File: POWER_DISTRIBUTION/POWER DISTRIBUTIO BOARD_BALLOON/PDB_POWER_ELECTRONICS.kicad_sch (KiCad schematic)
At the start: 45 parts, among them IC7 TPS56837RPAR, U3 MP3432GL-P

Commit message: POWER BOARD LAYOUT COMPLETE
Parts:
- removed F1: 0154005.DRL, SamacSys_Parts:0154005DRL, symbol SamacSys_Parts:0154005.DRL
- added F2: 0154005.DRL, SamacSys_Parts:0154005DRL, symbol SamacSys_Parts:0154005.DRL
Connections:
- net VBAT+: now also F2.1
- net VBAT_Fused: now reaches C13.2, C15.2, C17.2, C19.2, PS3.1 (+VIN)
- net VBAT_Fused: now also F2.2

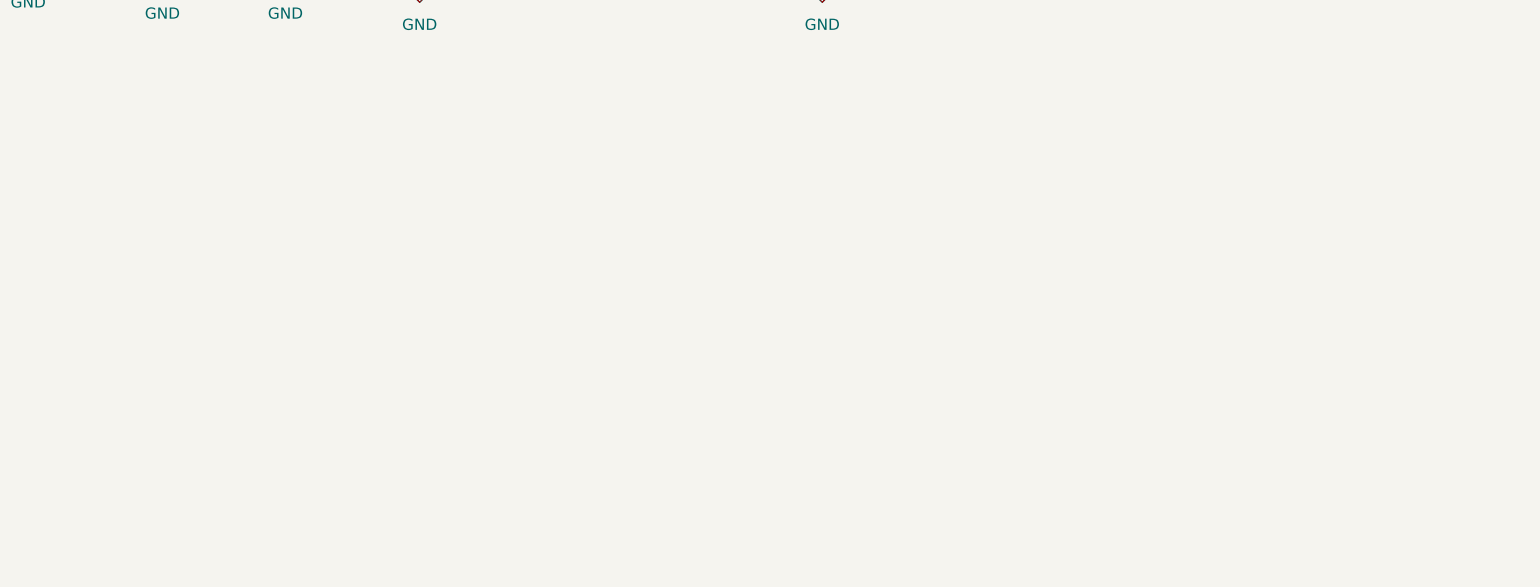
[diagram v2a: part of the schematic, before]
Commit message: almost finished wiring
btw for the i2c bus idk if it was meant to be SCL instead of SDL , there is alr an SDA line but i assume so
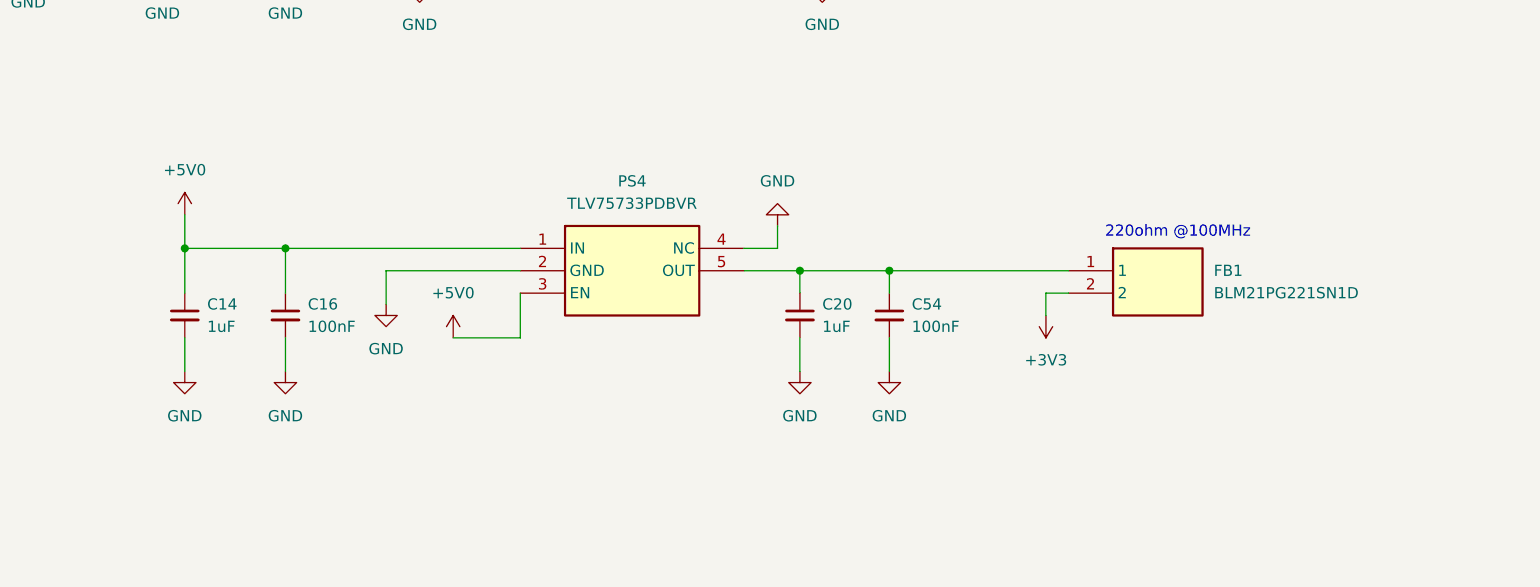
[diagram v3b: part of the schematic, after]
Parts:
- added C14, C20: 1uF, Capacitor_SMD:C_0603_1608Metric, symbol Device:C_Small
- added C16, C54: 100nF, Capacitor_SMD:C_0603_1608Metric, symbol Device:C_Small
- added FB1: BLM21PG221SN1D, SamacSys_COMMS:BEADC2012X105N, symbol Samac_sys:BLM21PG221SN1D
- added PS4: TLV75733PDBVR, SamacSys_COMMS:SOT95P280X145-5N, symbol Samac_sys:TLV75733PDBVR
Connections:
- net +5V0: now also C14.1, C16.1, PS4.1 (IN), PS4.3 (EN)
- net GND: now also C14.2, C16.2, C20.2, C54.2, PS4.2 (GND), PS4.4 (NC)
- new net: C20.1, C54.1, FB1.1, PS4.5 (OUT)
- new net +3V3: FB1.2
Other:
- note added: "220ohm @100MHz"

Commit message: revert commit
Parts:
- FB1: footprint SamacSys_COMMS:BEADC2012X105N -> SamacSys_Parts:BEADC2012X105N
- PS4: footprint SamacSys_COMMS:SOT95P280X145-5N -> SamacSys_Parts:SOT95P280X145-5N
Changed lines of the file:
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@@
 	)
 	(table
-		(column_count 1)
-		(border
-			(external yes)
-			(header yes)
-			(stroke
-				(width 0)
-				(type solid)
-			)
-		)
-		(separators
-			(rows yes)
-			(cols yes)
-			(stroke
-				(width 0)
-				(type solid)
-			)
-		)
-		(column_widths 19.05)
-		(row_heights -5.08)
-		(cells
-			(table_cell ""
-				(exclude_from_sim no)
-				(at 321.31 195.58 0)
-				(size 19.05 -5.08)
-				(margins 0.9525 0.9525 0.9525 0.9525)
-				(span 1 1)
-				(fill
-					(type none)
-				)
-				(effects
-					(font
-						(size 1.27 1.27)
-					)
-					(justify left top)
-				)
-			)
-		)
-	)
-	(table
 		(column_count 3)
 		(border
@@
 		)
 	)
+	(table
+		(column_count 1)
+		(border
+			(external yes)
+			(header yes)
+			(stroke
+				(width 0)
+				(type solid)
+			)
+		)
+		(separators
+			(rows yes)
+			(cols yes)
+			(stroke
+				(width 0)
+				(type solid)
+			)
+		)
+		(column_widths 19.05)
+		(row_heights -5.08)
+		(cells
+			(table_cell ""
+				(exclude_from_sim no)
+				(at 321.31 195.58 0)
+				(size 19.05 -5.08)
+				(margins 0.9525 0.9525 0.9525 0.9525)
+				(span 1 1)
+				(fill
+					(type none)
+				)
+				(effects
+					(font
+						(size 1.27 1.27)
+					)
+					(justify left top)
+				)
+			)
+		)
+	)
 	(global_label "MODE"
 		(shape output)
@@
 			)
 		)
-		(property "Footprint" "SamacSys_COMMS:BEADC2012X105N"
+		(property "Footprint" "SamacSys_Parts:BEADC2012X105N"
 			(at 186.69 178.74 0)
 			(effects
@@
 			)
 		)
-		(property "Footprint" "SamacSys_COMMS:SOT95P280X145-5N"
+		(property "Footprint" "SamacSys_Parts:SOT95P280X145-5N"
 			(at 129.54 176.2 0)
 			(effects

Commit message: test
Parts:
- FB1: footprint SamacSys_Parts:BEADC2012X105N -> SamacSys_COMMS:BEADC2012X105N
- PS4: footprint SamacSys_Parts:SOT95P280X145-5N -> SamacSys_COMMS:SOT95P280X145-5N
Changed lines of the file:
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@@
 	)
 	(table
+		(column_count 1)
+		(border
+			(external yes)
+			(header yes)
+			(stroke
+				(width 0)
+				(type solid)
+			)
+		)
+		(separators
+			(rows yes)
+			(cols yes)
+			(stroke
+				(width 0)
+				(type solid)
+			)
+		)
+		(column_widths 19.05)
+		(row_heights -5.08)
+		(cells
+			(table_cell ""
+				(exclude_from_sim no)
+				(at 321.31 195.58 0)
+				(size 19.05 -5.08)
+				(margins 0.9525 0.9525 0.9525 0.9525)
+				(span 1 1)
+				(fill
+					(type none)
+				)
+				(effects
+					(font
+						(size 1.27 1.27)
+					)
+					(justify left top)
+				)
+			)
+		)
+	)
+	(table
 		(column_count 3)
 		(border
@@
 		)
 	)
-	(table
-		(column_count 1)
-		(border
-			(external yes)
-			(header yes)
-			(stroke
-				(width 0)
-				(type solid)
-			)
-		)
-		(separators
-			(rows yes)
-			(cols yes)
-			(stroke
-				(width 0)
-				(type solid)
-			)
-		)
-		(column_widths 19.05)
-		(row_heights -5.08)
-		(cells
-			(table_cell ""
-				(exclude_from_sim no)
-				(at 321.31 195.58 0)
-				(size 19.05 -5.08)
-				(margins 0.9525 0.9525 0.9525 0.9525)
-				(span 1 1)
-				(fill
-					(type none)
-				)
-				(effects
-					(font
-						(size 1.27 1.27)
-					)
-					(justify left top)
-				)
-			)
-		)
-	)
 	(global_label "MODE"
 		(shape output)
@@
 			)
 		)
-		(property "Footprint" "SamacSys_Parts:BEADC2012X105N"
+		(property "Footprint" "SamacSys_COMMS:BEADC2012X105N"
 			(at 186.69 178.74 0)
 			(effects
@@
 			)
 		)
-		(property "Footprint" "SamacSys_Parts:SOT95P280X145-5N"
+		(property "Footprint" "SamacSys_COMMS:SOT95P280X145-5N"
 			(at 129.54 176.2 0)
 			(effects

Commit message: layout yweaks
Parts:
- FB1: footprint SamacSys_COMMS:BEADC2012X105N -> SamacSys_Parts:BEADC2012X105N
- PS4: footprint SamacSys_COMMS:SOT95P280X145-5N -> SamacSys_Parts:SOT95P280X145-5N
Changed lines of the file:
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@@
 			)
 		)
-		(property "Footprint" "SamacSys_COMMS:BEADC2012X105N"
+		(property "Footprint" "SamacSys_Parts:BEADC2012X105N"
 			(at 186.69 178.74 0)
 			(effects
@@
 			)
 		)
-		(property "Footprint" "SamacSys_COMMS:SOT95P280X145-5N"
+		(property "Footprint" "SamacSys_Parts:SOT95P280X145-5N"
 			(at 129.54 176.2 0)
 			(effects
